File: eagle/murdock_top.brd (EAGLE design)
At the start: 47 x 31.8 mm, 35 parts, among them IC1 74HC595D, IC2 74HC595D, X1 MURDOCK_STACK

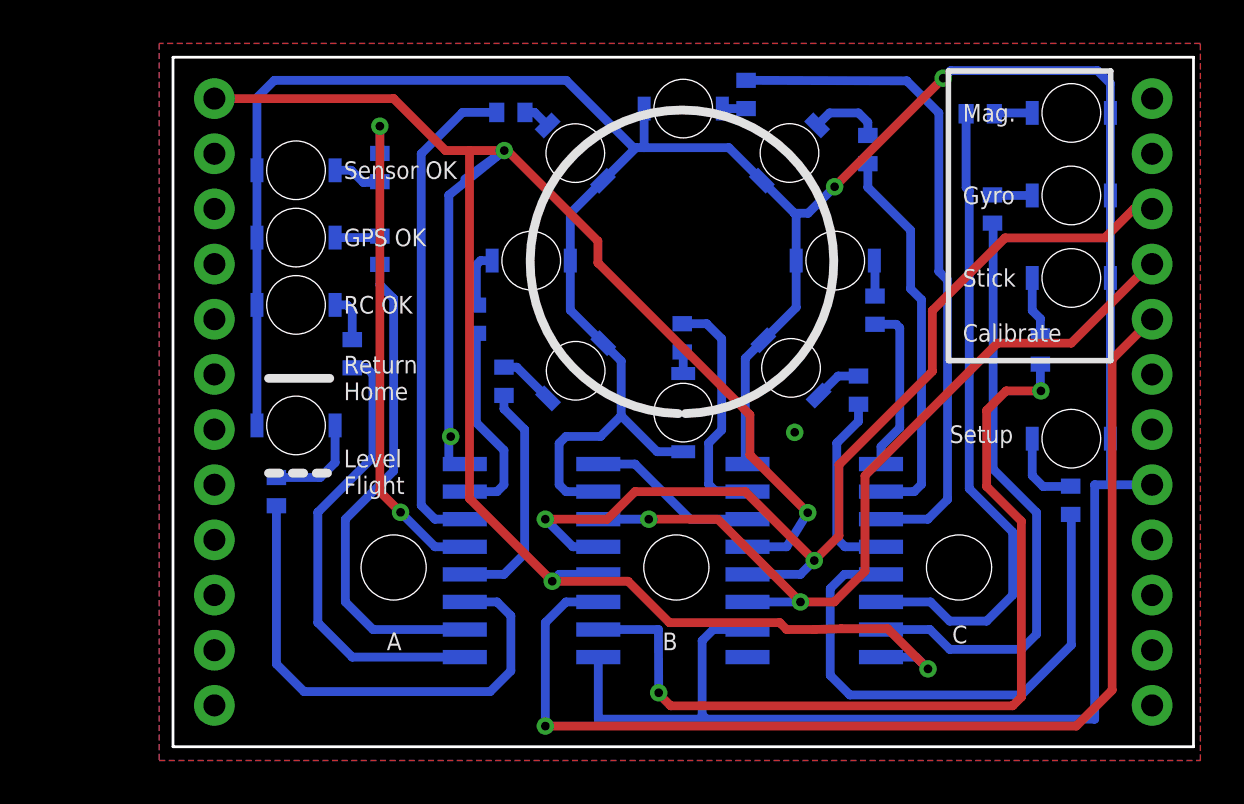
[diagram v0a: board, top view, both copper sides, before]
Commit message: LED positions beautified
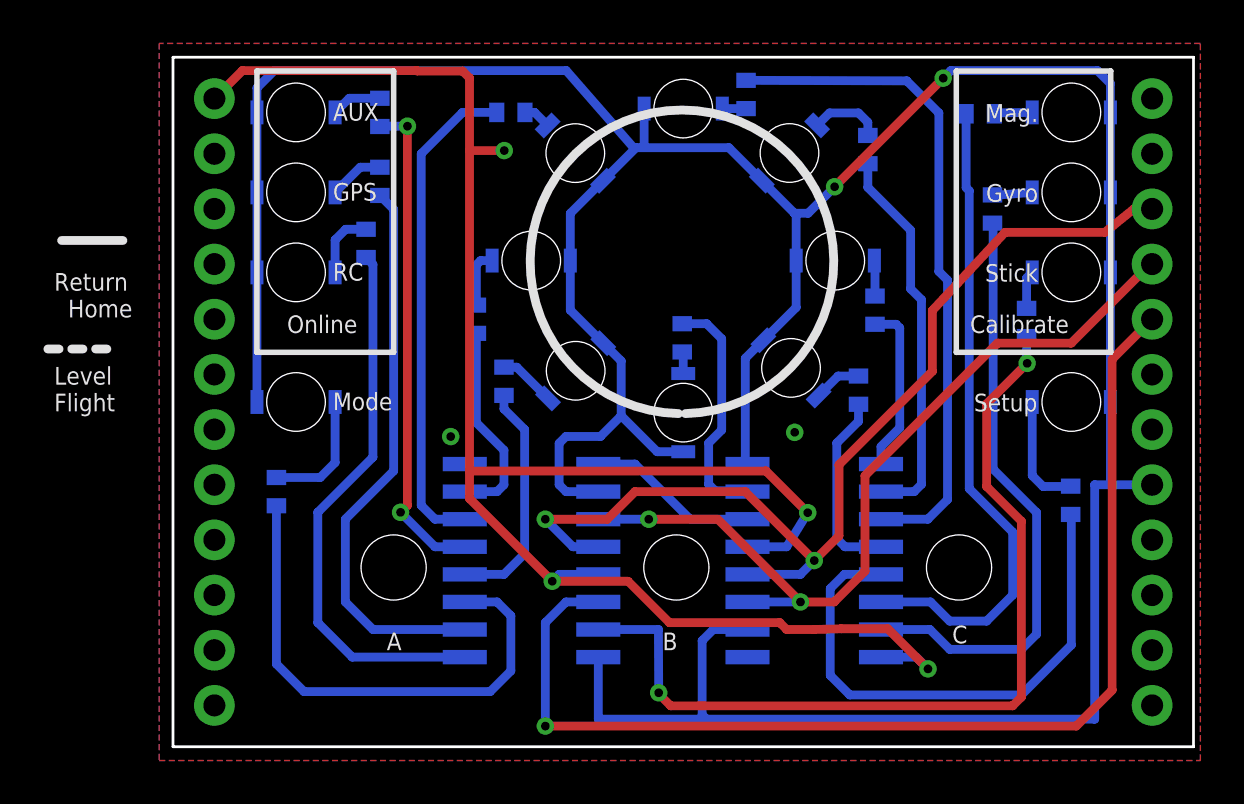
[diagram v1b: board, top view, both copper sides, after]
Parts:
- moved R15 5.12 mm to (8.89, 23.2)
- moved R14 3.18 mm to (9.53, 26.0)
- moved LED6 2.66 mm to (5.67, 29.2)
- moved R11 2.54 mm to (9.53, 29.2), turned to 90 degrees
- moved LED3 2.08 mm to (5.67, 25.5)
- moved LED14 1.69 mm to (41.4, 15.9)
- moved LED2 1.50 mm to (5.67, 21.8)
- moved R16 1.42 mm to (39.3, 19.5)
- moved LED4 1.08 mm to (5.67, 15.9)
- moved LED1 0.26 mm to (41.4, 21.8)
- moved LED16 0.14 mm to (41.4, 25.5)
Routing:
- net GND: track 104.2 -> 83.3 mm
- net QB: track 21.0 -> 25.4 mm
- net QC: track 22.8 -> 25.9 mm
- net N$7: track 3.68 -> 5.37 mm
- net N$13: track 4.70 -> 5.78 mm
- net N$10: track 2.82 -> 1.76 mm
- net N$11: track 2.24 -> 3.12 mm
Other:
- board text added: "AUX"
- board text added: "GPS"
- board text added: "Mode"
- board text added: "Online"
- board text added: "RC"
- board text removed: "GPS OK"
- board text removed: "RC OK"
- board text removed: "Sensor OK"

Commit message: final fixes for 1st production run
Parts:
- moved R2 0.80 mm to (32.3, 19.3)
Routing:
- net Q1: track 7.83 -> 7.03 mm
- net N$3: track 1.64 -> 2.44 mm
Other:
- board text added: "AUX OK"
- board text added: "GPS OK"
- board text added: "Mag"
- board text added: "RC OK"
- board text removed: "AUX"
- board text removed: "GPS"
- board text removed: "Mag."
- board text removed: "Mode"
- board text removed: "Online"
- board text removed: "RC"
